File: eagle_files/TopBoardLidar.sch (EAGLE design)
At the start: 15 parts, among them U2 52207-0485, U3 VL53L1XSMD

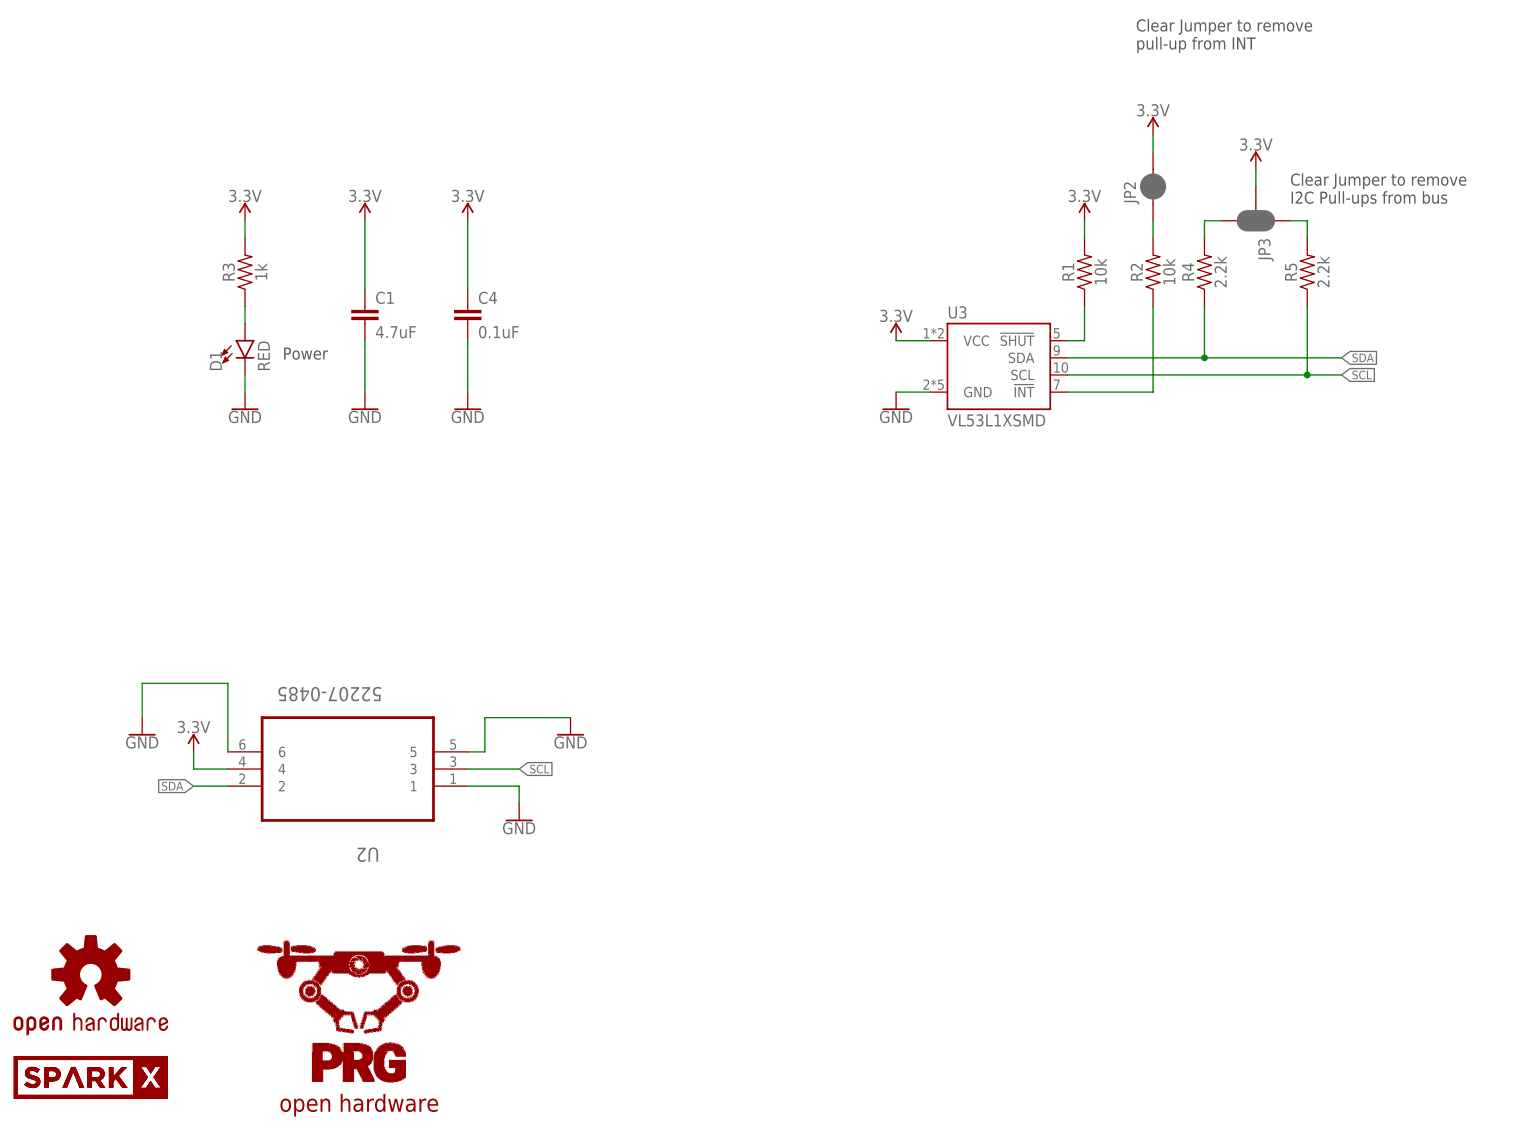
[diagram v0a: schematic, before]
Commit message: top layer board routing
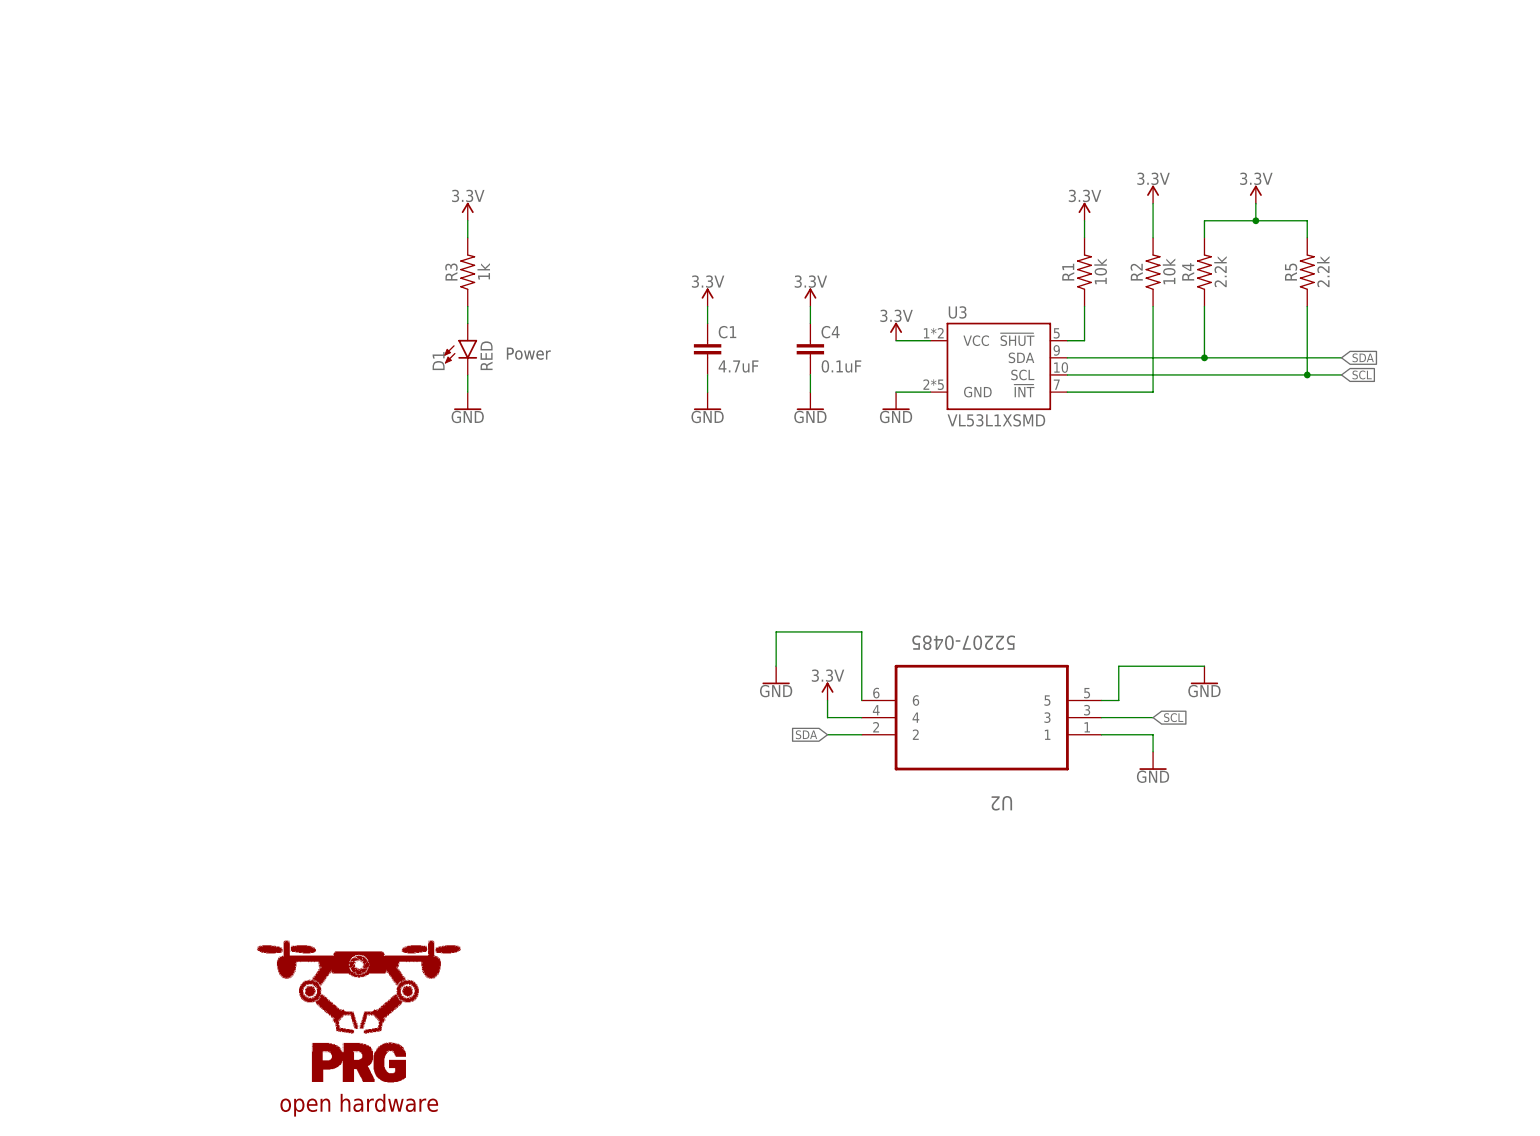
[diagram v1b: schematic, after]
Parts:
- removed JP2: JUMPER-SMT_2_NC_PASTE_NO-SILK, SparkFun-Jumpers:JUMPER-SMT_2_NC_PASTE_NO-SILK
- removed JP3: JUMPER-SMT_3_2-NC_PASTE_NO-SILK, SparkFun-Jumpers:JUMPER-SMT_3_2-NC_PASTE_NO-SILK
- removed LOGO1: OSHW-LOGOMINI, SparkFun-Aesthetics:OSHW-LOGOMINI
- removed U$1, U$2: SPARKX-LOGO4, SparkX:SPARKX-LOGO4
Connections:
- removed net N$10: JP3.1, R5.2
- removed net N$11: JP3.3, R4.2
- removed net N$9: JP2.1, R2.2
- net 3.3V: now also R2.2, R4.2, R5.2; no longer JP2.2, JP3.2
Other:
- note removed: "Clear Jumper to remove I2C Pull-ups from bus"
- note removed: "Clear Jumper to remove pull-up from INT"
- moved on the sheet: C1, C4, D1, R3, U2
